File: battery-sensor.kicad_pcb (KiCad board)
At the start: 2 copper layers, 93.5 x 74.5 mm, 22 parts, among them J1 Conn_01x06_Pin, J10 Conn_01x03_Pin, J2 Conn_01x06_Pin, J3 Conn_01x06_Pin, J4 Conn_01x08_Pin, J5 Conn_01x06_Pin, J6 Conn_01x02_Pin, J7 Conn_01x02_Pin, J8 Conn_01x02_Pin, J9 Conn_01x02_Pin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

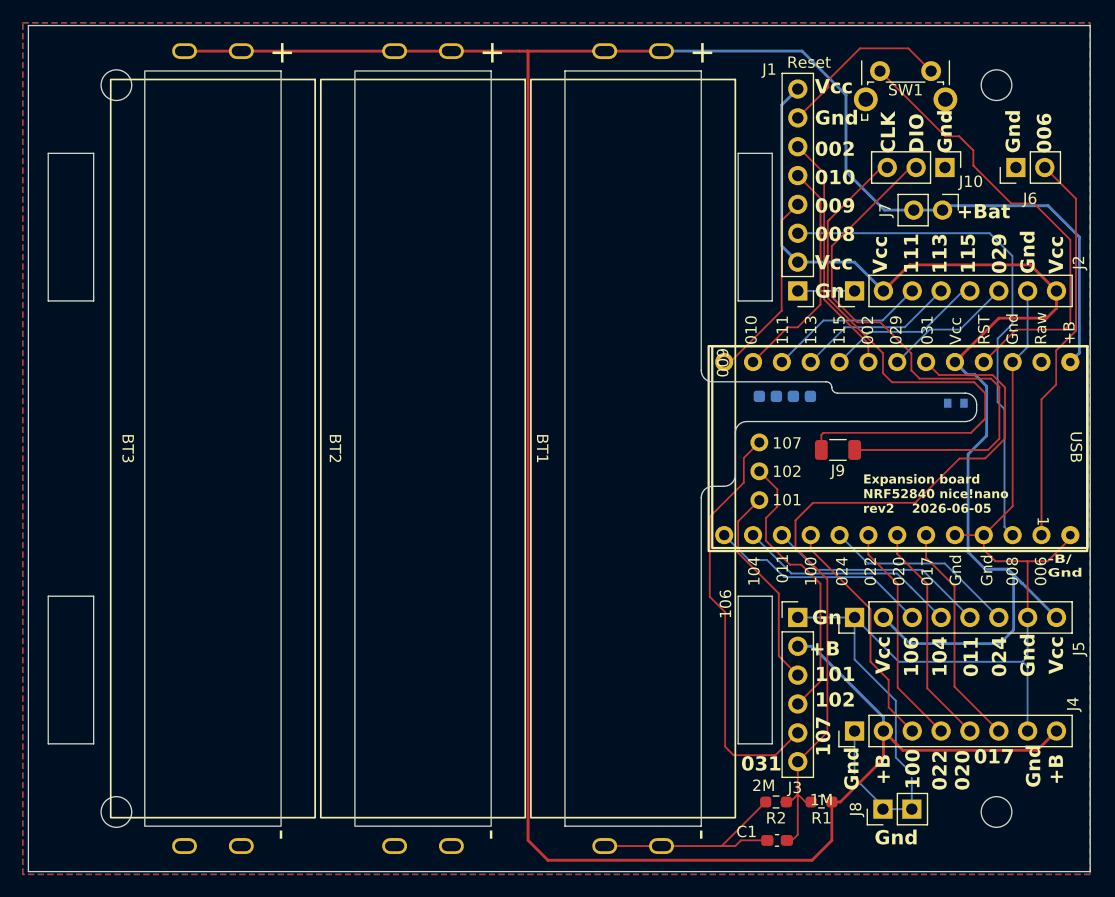
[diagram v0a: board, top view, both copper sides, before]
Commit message: Increase mounting hole size to account for small size variations of the plastic enclosures.
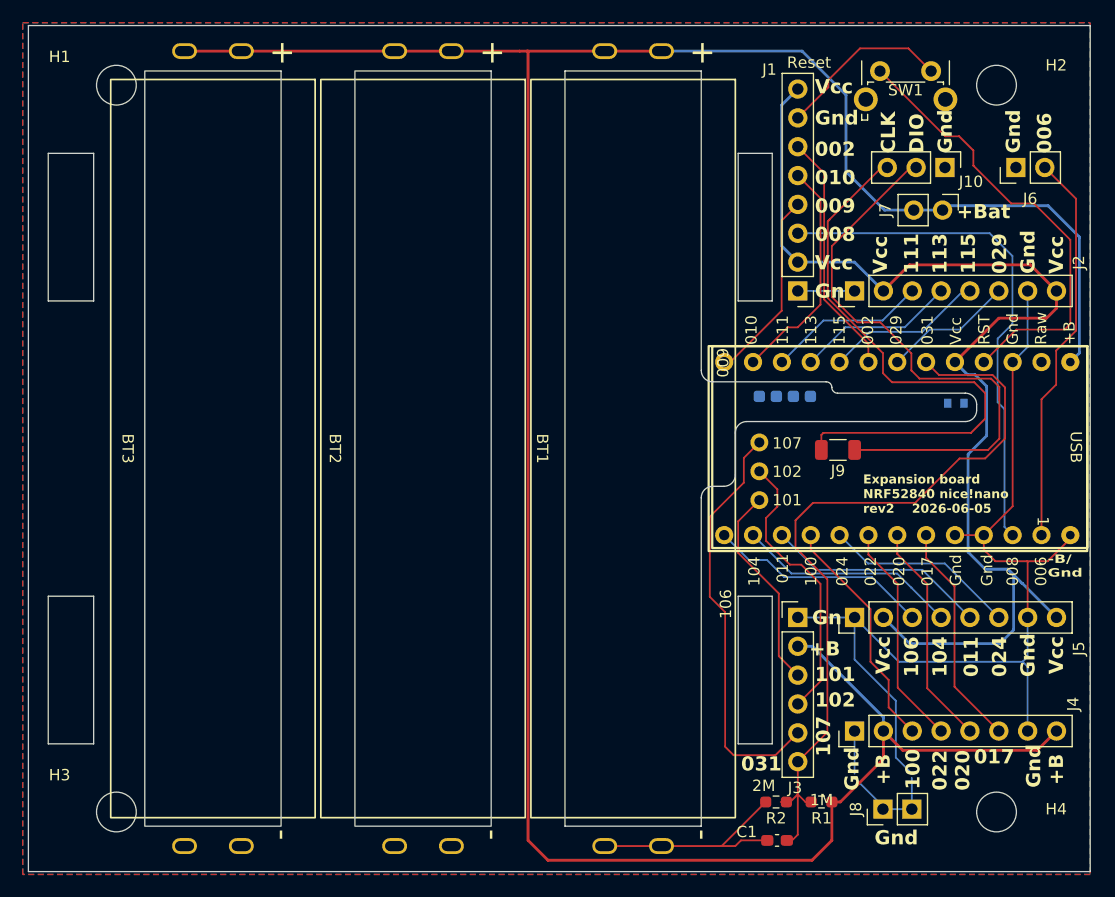
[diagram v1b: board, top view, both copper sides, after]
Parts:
- H1, H2, H3, H4: footprint MountingHole:MountingHole_2.7mm_M2.5_ISO7380 -> MountingHole:MountingHole_3.5mm
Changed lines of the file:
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@@
 		)
 	)
-	(footprint "MountingHole:MountingHole_2.7mm_M2.5_ISO7380"
+	(footprint "MountingHole:MountingHole_3.5mm"
 		(locked yes)
 		(layer "F.Cu")
 		(at 127.5 104)
-		(descr "Mounting Hole 2.7mm, M2.5, no annular, generated by kicad-footprint-generator mountinghole.py")
-		(tags "mountinghole M2.5 ISO7380")
+		(descr "Mounting Hole 3.5mm, no annular, generated by kicad-footprint-generator mountinghole.py")
+		(tags "mountinghole")
 		(property "Reference" "H4"
-			(at 0 -1.95 0)
-			(layer "F.Fab")
+			(at 5.25 -0.25 0)
+			(layer "F.SilkS")
 			(effects
 				(font
@@
 		)
 		(property "Value" "MountingHole"
-			(at 0 3.2 0)
+			(at 0 4.45 0)
 			(layer "F.Fab")
 			(effects
@@
 				(font
 					(size 1.27 1.27)
-					(thickness 0.15)
 				)
 			)
@@
 				(font
 					(size 1.27 1.27)
+				)
+			)
+		)
+		(property "KiLib_Generator" "mounting_hardware/mounting_hole"
+			(at 0 0 0)
+			(layer "F.SilkS")
+			(hide yes)
+			(effects
+				(font
+					(size 1 1)
 					(thickness 0.15)
 				)
@@
 		(fp_circle
 			(center 0 0)
-			(end 2.25 0)
+			(end 3.5 0)
 			(stroke
 				(width 0.15)
@@
 		(fp_circle
 			(center 0 0)
-			(end 2.5 0)
+			(end 3.75 0)
 			(stroke
 				(width 0.05)
@@
 		(pad "" np_thru_hole circle
 			(at 0 0)
-			(size 2.7 2.7)
-			(drill 2.7)
+			(size 3.5 3.5)
+			(drill 3.5)
 			(layers "*.Cu" "*.Mask")
 		)
@@
 		(embedded_fonts no)
 	)
-	(footprint "MountingHole:MountingHole_2.7mm_M2.5_ISO7380"
+	(footprint "MountingHole:MountingHole_3.5mm"
 		(locked yes)
 		(layer "F.Cu")
 		(at 127.5 40)
-		(descr "Mounting Hole 2.7mm, M2.5, no annular, generated by kicad-footprint-generator mountinghole.py")
-		(tags "mountinghole M2.5 ISO7380")
+		(descr "Mounting Hole 3.5mm, no annular, generated by kicad-footprint-generator mountinghole.py")
+		(tags "mountinghole")
 		(property "Reference" "H2"
-			(at 0 -3.2 0)
-			(layer "F.Fab")
+			(at 5.25 -1.75 0)
+			(layer "F.SilkS")
 			(effects
 				(font
@@
 		)
 		(property "Value" "MountingHole"
-			(at -0.04 4.08 0)
+			(at 0 4.45 0)
 			(layer "F.Fab")
 			(effects
@@
 				(font
 					(size 1.27 1.27)
-					(thickness 0.15)
 				)
 			)
@@
 				(font
 					(size 1.27 1.27)
+				)
+			)
+		)
+		(property "KiLib_Generator" "mounting_hardware/mounting_hole"
+			(at 0 0 0)
+			(layer "F.SilkS")
+			(hide yes)
+			(effects
+				(font
+					(size 1 1)
 					(thickness 0.15)
 				)
@@
 		(fp_circle
 			(center 0 0)
-			(end 2.25 0)
+			(end 3.5 0)
 			(stroke
 				(width 0.15)
@@
 		(fp_circle
 			(center 0 0)
-			(end 2.5 0)
+			(end 3.75 0)
 			(stroke
 				(width 0.05)
@@
 		(pad "" np_thru_hole circle
 			(at 0 0)
-			(size 2.7 2.7)
-			(drill 2.7)
+			(size 3.5 3.5)
+			(drill 3.5)
 			(layers "*.Cu" "*.Mask")
 		)
@@
 		)
 	)
-	(footprint "MountingHole:MountingHole_2.7mm_M2.5_ISO7380"
+	(footprint "MountingHole:MountingHole_3.5mm"
+		(locked yes)
 		(layer "F.Cu")
 		(at 50 40)
-		(descr "Mounting Hole 2.7mm, M2.5, no annular, generated by kicad-footprint-generator mountinghole.py")
-		(tags "mountinghole M2.5 ISO7380")
+		(descr "Mounting Hole 3.5mm, no annular, generated by kicad-footprint-generator mountinghole.py")
+		(tags "mountinghole")
 		(property "Reference" "H1"
-			(at 0 -3.2 0)
-			(layer "F.Fab")
+			(at -5 -2.5 0)
+			(layer "F.SilkS")
 			(effects
 				(font
@@
 		)
 		(property "Value" "MountingHole"
-			(at 0 3.2 0)
+			(at 0 4.45 0)
 			(layer "F.Fab")
 			(effects
@@
 				(font
 					(size 1.27 1.27)
-					(thickness 0.15)
 				)
 			)
@@
 				(font
 					(size 1.27 1.27)
+				)
+			)
+		)
+		(property "KiLib_Generator" "mounting_hardware/mounting_hole"
+			(at 0 0 0)
+			(layer "F.SilkS")
+			(hide yes)
+			(effects
+				(font
+					(size 1 1)
 					(thickness 0.15)
 				)
@@
 		(fp_circle
 			(center 0 0)
-			(end 2.25 0)
+			(end 3.5 0)
 			(stroke
 				(width 0.15)
@@
 		(fp_circle
 			(center 0 0)
-			(end 2.5 0)
+			(end 3.75 0)
 			(stroke
 				(width 0.05)
@@
 		(pad "" np_thru_hole circle
 			(at 0 0)
-			(size 2.7 2.7)
-			(drill 2.7)
+			(size 3.5 3.5)
+			(drill 3.5)
 			(layers "*.Cu" "*.Mask")
 		)
@@
 		)
 	)
-	(footprint "MountingHole:MountingHole_2.7mm_M2.5_ISO7380"
+	(footprint "MountingHole:MountingHole_3.5mm"
+		(locked yes)
 		(layer "F.Cu")
 		(at 50 104)
-		(descr "Mounting Hole 2.7mm, M2.5, no annular, generated by kicad-footprint-generator mountinghole.py")
-		(tags "mountinghole M2.5 ISO7380")
+		(descr "Mounting Hole 3.5mm, no annular, generated by kicad-footprint-generator mountinghole.py")
+		(tags "mountinghole")
 		(property "Reference" "H3"
-			(at -2.25 -3 0)
-			(layer "F.Fab")
+			(at -5 -3.25 0)
+			(layer "F.SilkS")
 			(effects
 				(font
@@
 		)
 		(property "Value" "MountingHole"
-			(at 0 3.2 0)
+			(at 0 4.45 0)
 			(layer "F.Fab")
 			(effects
@@
 				(font
 					(size 1.27 1.27)
-					(thickness 0.15)
 				)
 			)
@@
 				(font
 					(size 1.27 1.27)
+				)
+			)
+		)
+		(property "KiLib_Generator" "mounting_hardware/mounting_hole"
+			(at 0 0 0)
+			(layer "F.SilkS")
+			(hide yes)
+			(effects
+				(font
+					(size 1 1)
 					(thickness 0.15)
 				)
@@
 		(fp_circle
 			(center 0 0)
-			(end 2.25 0)
+			(end 3.5 0)
 			(stroke
 				(width 0.15)
@@
 		(fp_circle
 			(center 0 0)
-			(end 2.5 0)
+			(end 3.75 0)
 			(stroke
 				(width 0.05)
@@
 		(pad "" np_thru_hole circle
 			(at 0 0)
-			(size 2.7 2.7)
-			(drill 2.7)
+			(size 3.5 3.5)
+			(drill 3.5)
 			(layers "*.Cu" "*.Mask")
 		)
